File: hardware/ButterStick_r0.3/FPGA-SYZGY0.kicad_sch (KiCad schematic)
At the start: 1 part, among them U4 ECP5UM5G_85_CABGA381

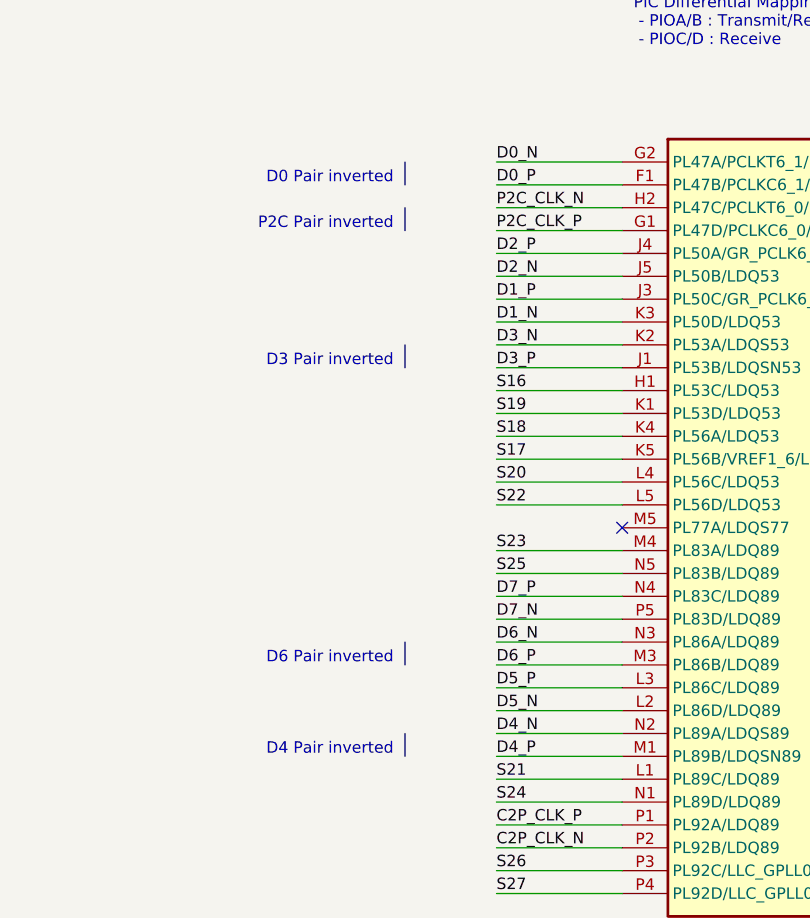
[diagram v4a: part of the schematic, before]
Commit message: hw.r0d3: Length matched all SYZYGY ports
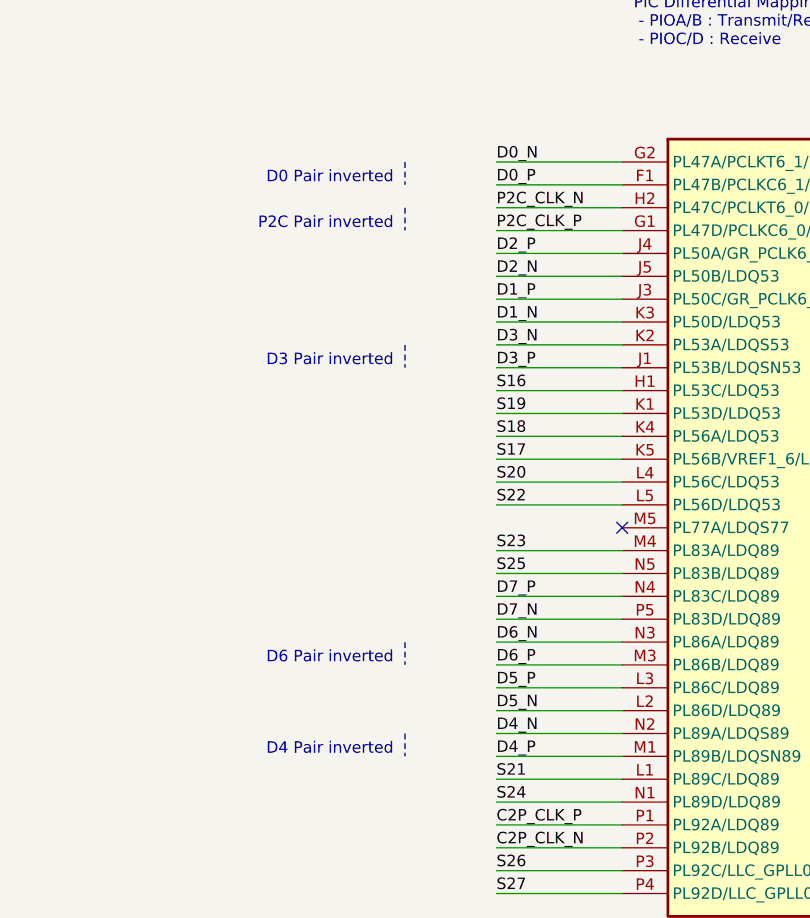
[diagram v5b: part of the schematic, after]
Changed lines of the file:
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@@
-(kicad_sch (version 20200512) (host eeschema "5.99.0-unknown-711fc99~101~ubuntu18.04.1")
+(kicad_sch (version 20200608) (host eeschema "5.99.0-unknown-08c61e6~101~ubuntu18.04.1")
   (page 1 19)
   (paper "A4")
   (no_connect (at 132.08 109.22))
   (bus_entry (at 116.84 49.53) (size 2.54 -2.54))
-  (wire (pts (xy 118.11 68.58) (xy 132.08 68.58)))
-  (wire (pts (xy 118.11 71.12) (xy 132.08 71.12)))
-  (wire (pts (xy 118.11 73.66) (xy 132.08 73.66)))
-  (wire (pts (xy 118.11 76.2) (xy 132.08 76.2)))
-  (wire (pts (xy 118.11 78.74) (xy 132.08 78.74)))
-  (wire (pts (xy 118.11 81.28) (xy 132.08 81.28)))
-  (wire (pts (xy 118.11 83.82) (xy 132.08 83.82)))
-  (wire (pts (xy 118.11 86.36) (xy 132.08 86.36)))
-  (wire (pts (xy 118.11 88.9) (xy 132.08 88.9)))
-  (wire (pts (xy 118.11 91.44) (xy 132.08 91.44)))
-  (wire (pts (xy 118.11 93.98) (xy 132.08 93.98)))
-  (wire (pts (xy 118.11 96.52) (xy 132.08 96.52)))
-  (wire (pts (xy 118.11 99.06) (xy 132.08 99.06)))
-  (wire (pts (xy 118.11 101.6) (xy 132.08 101.6)))
-  (wire (pts (xy 118.11 104.14) (xy 132.08 104.14)))
-  (wire (pts (xy 118.11 106.68) (xy 132.08 106.68)))
-  (wire (pts (xy 118.11 111.76) (xy 132.08 111.76)))
-  (wire (pts (xy 118.11 114.3) (xy 132.08 114.3)))
-  (wire (pts (xy 118.11 116.84) (xy 132.08 116.84)))
-  (wire (pts (xy 118.11 119.38) (xy 132.08 119.38)))
-  (wire (pts (xy 118.11 121.92) (xy 132.08 121.92)))
-  (wire (pts (xy 118.11 124.46) (xy 132.08 124.46)))
-  (wire (pts (xy 118.11 127) (xy 132.08 127)))
-  (wire (pts (xy 118.11 129.54) (xy 132.08 129.54)))
-  (wire (pts (xy 118.11 132.08) (xy 132.08 132.08)))
-  (wire (pts (xy 118.11 134.62) (xy 132.08 134.62)))
-  (wire (pts (xy 118.11 137.16) (xy 132.08 137.16)))
-  (wire (pts (xy 118.11 139.7) (xy 132.08 139.7)))
-  (wire (pts (xy 118.11 142.24) (xy 132.08 142.24)))
-  (wire (pts (xy 118.11 144.78) (xy 132.08 144.78)))
-  (wire (pts (xy 118.11 147.32) (xy 132.08 147.32)))
-  (wire (pts (xy 118.11 149.86) (xy 132.08 149.86)))
-  (wire (pts (xy 119.38 46.99) (xy 170.18 46.99)))
-  (wire (pts (xy 170.18 46.99) (xy 170.18 60.96)))
-  (bus (pts (xy 45.72 49.53) (xy 119.38 49.53)))
-  (polyline (pts (xy 107.95 68.58) (xy 107.95 71.12)))
-  (polyline (pts (xy 107.95 73.66) (xy 107.95 76.2)))
-  (polyline (pts (xy 107.95 88.9) (xy 107.95 91.44)))
-  (polyline (pts (xy 107.95 121.92) (xy 107.95 124.46)))
-  (polyline (pts (xy 107.95 132.08) (xy 107.95 134.62)))
+  (wire (pts (xy 118.11 68.58) (xy 132.08 68.58))
+    (stroke (width 0) (type solid) (color 0 0 0 0))
+  )
+  (wire (pts (xy 118.11 71.12) (xy 132.08 71.12))
+    (stroke (width 0) (type solid) (color 0 0 0 0))
+  )
+  (wire (pts (xy 118.11 73.66) (xy 132.08 73.66))
+    (stroke (width 0) (type solid) (color 0 0 0 0))
+  )
+  (wire (pts (xy 118.11 76.2) (xy 132.08 76.2))
+    (stroke (width 0) (type solid) (color 0 0 0 0))
+  )
+  (wire (pts (xy 118.11 78.74) (xy 132.08 78.74))
+    (stroke (width 0) (type solid) (color 0 0 0 0))
+  )
+  (wire (pts (xy 118.11 81.28) (xy 132.08 81.28))
+    (stroke (width 0) (type solid) (color 0 0 0 0))
+  )
+  (wire (pts (xy 118.11 83.82) (xy 132.08 83.82))
+    (stroke (width 0) (type solid) (color 0 0 0 0))
+  )
+  (wire (pts (xy 118.11 86.36) (xy 132.08 86.36))
+    (stroke (width 0) (type solid) (color 0 0 0 0))
+  )
+  (wire (pts (xy 118.11 88.9) (xy 132.08 88.9))
+    (stroke (width 0) (type solid) (color 0 0 0 0))
+  )
+  (wire (pts (xy 118.11 91.44) (xy 132.08 91.44))
+    (stroke (width 0) (type solid) (color 0 0 0 0))
+  )
+  (wire (pts (xy 118.11 93.98) (xy 132.08 93.98))
+    (stroke (width 0) (type solid) (color 0 0 0 0))
+  )
+  (wire (pts (xy 118.11 96.52) (xy 132.08 96.52))
+    (stroke (width 0) (type solid) (color 0 0 0 0))
+  )
+  (wire (pts (xy 118.11 99.06) (xy 132.08 99.06))
+    (stroke (width 0) (type solid) (color 0 0 0 0))
+  )
+  (wire (pts (xy 118.11 101.6) (xy 132.08 101.6))
+    (stroke (width 0) (type solid) (color 0 0 0 0))
+  )
+  (wire (pts (xy 118.11 104.14) (xy 132.08 104.14))
+    (stroke (width 0) (type solid) (color 0 0 0 0))
+  )
+  (wire (pts (xy 118.11 106.68) (xy 132.08 106.68))
+    (stroke (width 0) (type solid) (color 0 0 0 0))
+  )
+  (wire (pts (xy 118.11 111.76) (xy 132.08 111.76))
+    (stroke (width 0) (type solid) (color 0 0 0 0))
+  )
+  (wire (pts (xy 118.11 114.3) (xy 132.08 114.3))
+    (stroke (width 0) (type solid) (color 0 0 0 0))
+  )
+  (wire (pts (xy 118.11 116.84) (xy 132.08 116.84))
+    (stroke (width 0) (type solid) (color 0 0 0 0))
+  )
+  (wire (pts (xy 118.11 119.38) (xy 132.08 119.38))
+    (stroke (width 0) (type solid) (color 0 0 0 0))
+  )
+  (wire (pts (xy 118.11 121.92) (xy 132.08 121.92))
+    (stroke (width 0) (type solid) (color 0 0 0 0))
+  )
+  (wire (pts (xy 118.11 124.46) (xy 132.08 124.46))
+    (stroke (width 0) (type solid) (color 0 0 0 0))
+  )
+  (wire (pts (xy 118.11 127) (xy 132.08 127))
+    (stroke (width 0) (type solid) (color 0 0 0 0))
+  )
+  (wire (pts (xy 118.11 129.54) (xy 132.08 129.54))
+    (stroke (width 0) (type solid) (color 0 0 0 0))
+  )
+  (wire (pts (xy 118.11 132.08) (xy 132.08 132.08))
+    (stroke (width 0) (type solid) (color 0 0 0 0))
+  )
+  (wire (pts (xy 118.11 134.62) (xy 132.08 134.62))
+    (stroke (width 0) (type solid) (color 0 0 0 0))
+  )
+  (wire (pts (xy 118.11 137.16) (xy 132.08 137.16))
+    (stroke (width 0) (type solid) (color 0 0 0 0))
+  )
+  (wire (pts (xy 118.11 139.7) (xy 132.08 139.7))
+    (stroke (width 0) (type solid) (color 0 0 0 0))
+  )
+  (wire (pts (xy 118.11 142.24) (xy 132.08 142.24))
+    (stroke (width 0) (type solid) (color 0 0 0 0))
+  )
+  (wire (pts (xy 118.11 144.78) (xy 132.08 144.78))
+    (stroke (width 0) (type solid) (color 0 0 0 0))
+  )
+  (wire (pts (xy 118.11 147.32) (xy 132.08 147.32))
+    (stroke (width 0) (type solid) (color 0 0 0 0))
+  )
+  (wire (pts (xy 118.11 149.86) (xy 132.08 149.86))
+    (stroke (width 0) (type solid) (color 0 0 0 0))
+  )
+  (wire (pts (xy 119.38 46.99) (xy 170.18 46.99))
+    (stroke (width 0) (type solid) (color 0 0 0 0))
+  )
+  (wire (pts (xy 170.18 46.99) (xy 170.18 60.96))
+    (stroke (width 0) (type solid) (color 0 0 0 0))
+  )
+  (bus (pts (xy 45.72 49.53) (xy 119.38 49.53))
+    (stroke (width 0) (type solid) (color 0 0 0 0))
+  )
+  (polyline (pts (xy 107.95 68.58) (xy 107.95 71.12))
+    (stroke (width 0) (type dash) (color 0 0 0 0))
+  )
+  (polyline (pts (xy 107.95 73.66) (xy 107.95 76.2))
+    (stroke (width 0) (type dash) (color 0 0 0 0))
+  )
+  (polyline (pts (xy 107.95 88.9) (xy 107.95 91.44))
+    (stroke (width 0) (type dash) (color 0 0 0 0))
+  )
+  (polyline (pts (xy 107.95 121.92) (xy 107.95 124.46))
+    (stroke (width 0) (type dash) (color 0 0 0 0))
+  )
+  (polyline (pts (xy 107.95 132.08) (xy 107.95 134.62))
+    (stroke (width 0) (type dash) (color 0 0 0 0))
+  )
   (text "D0 Pair inverted" (at 106.68 71.12 180)
     (effects (font (size 1.27 1.27)) (justify right bottom))
@@
   )
   (symbol (lib_id "gkl_lattice:ECP5UM5G_85_CABGA381") (at 132.08 68.58 0) (unit 6)
+    (in_bom yes) (on_board yes)
     (property "Reference" "U4" (id 0) (at 178.5874 97.5614 0)
       (effects (font (size 1.524 1.524)) (justify left))

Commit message: hw.r0d3: complete first pass of routing
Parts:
- added C25: 100nF, Capacitor_SMD:C_0402_1005Metric, symbol Device:C
- added C26: 10nF, Capacitor_SMD:C_0402_1005Metric, symbol Device:C
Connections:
- net VIO1: now also C25.1, C26.1
- new net GND: C25.2, C26.2
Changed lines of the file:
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@@
-(kicad_sch (version 20200608) (host eeschema "5.99.0-unknown-08c61e6~101~ubuntu18.04.1")
-  (page 1 19)
+(kicad_sch (version 20200618) (host eeschema "5.99.0-unknown-476558e~101~ubuntu18.04.1")
+  (page 9 19)
   (paper "A4")
+  (junction (at 170.18 53.34) (diameter 0) (color 0 0 0 0))
+  (junction (at 179.07 59.69) (diameter 0) (color 0 0 0 0))
   (no_connect (at 132.08 109.22))
-  (bus_entry (at 116.84 49.53) (size 2.54 -2.54))
+  (bus_entry (at 116.84 49.53) (size 2.54 -2.54)
+    (stroke (width 0.1524) (type solid) (color 0 0 0 0))
+  )
   (wire (pts (xy 118.11 68.58) (xy 132.08 68.58))
     (stroke (width 0) (type solid) (color 0 0 0 0))
@@
     (stroke (width 0) (type solid) (color 0 0 0 0))
   )
-  (wire (pts (xy 170.18 46.99) (xy 170.18 60.96))
+  (wire (pts (xy 170.18 46.99) (xy 170.18 53.34))
+    (stroke (width 0) (type solid) (color 0 0 0 0))
+  )
+  (wire (pts (xy 170.18 53.34) (xy 170.18 60.96))
+    (stroke (width 0) (type solid) (color 0 0 0 0))
+  )
+  (wire (pts (xy 170.18 53.34) (xy 179.07 53.34))
+    (stroke (width 0) (type solid) (color 0 0 0 0))
+  )
+  (wire (pts (xy 179.07 53.34) (xy 179.07 59.69))
+    (stroke (width 0) (type solid) (color 0 0 0 0))
+  )
+  (wire (pts (xy 179.07 59.69) (xy 179.07 60.96))
+    (stroke (width 0) (type solid) (color 0 0 0 0))
+  )
+  (wire (pts (xy 179.07 59.69) (xy 189.23 59.69))
+    (stroke (width 0) (type solid) (color 0 0 0 0))
+  )
+  (wire (pts (xy 179.07 68.58) (xy 179.07 69.85))
+    (stroke (width 0) (type solid) (color 0 0 0 0))
+  )
+  (wire (pts (xy 189.23 60.96) (xy 189.23 59.69))
+    (stroke (width 0) (type solid) (color 0 0 0 0))
+  )
+  (wire (pts (xy 189.23 69.85) (xy 189.23 68.58))
     (stroke (width 0) (type solid) (color 0 0 0 0))
   )
@@
     (effects (font (size 1.27 1.27)) (justify right))
   )
+  (symbol (lib_id "gkl_power:GND") (at 179.07 69.85 0) (unit 1)
+    (in_bom yes) (on_board yes)
+    (property "Reference" "#PWR0210" (id 0) (at 179.07 76.2 0)
+      (effects (font (size 1.27 1.27)) hide)
+    )
+    (property "Value" "GND" (id 1) (at 179.1462 73.0504 0))
+    (property "Footprint" "" (id 2) (at 176.53 78.74 0)
+      (effects (font (size 1.27 1.27)) hide)
+    )
+    (property "Datasheet" "" (id 3) (at 179.07 69.85 0)
+      (effects (font (size 1.27 1.27)) hide)
+    )
+  )
+  (symbol (lib_id "gkl_power:GND") (at 189.23 69.85 0) (unit 1)
+    (in_bom yes) (on_board yes)
+    (property "Reference" "#PWR0211" (id 0) (at 189.23 76.2 0)
+      (effects (font (size 1.27 1.27)) hide)
+    )
+    (property "Value" "GND" (id 1) (at 189.3062 73.0504 0))
+    (property "Footprint" "" (id 2) (at 186.69 78.74 0)
+      (effects (font (size 1.27 1.27)) hide)
+    )
+    (property "Datasheet" "" (id 3) (at 189.23 69.85 0)
+      (effects (font (size 1.27 1.27)) hide)
+    )
+  )
+  (symbol (lib_id "Device:C") (at 179.07 64.77 0) (unit 1)
+    (in_bom yes) (on_board yes)
+    (property "Reference" "C25" (id 0) (at 180.34 62.23 0)
+      (effects (font (size 1.27 1.27)) (justify left))
+    )
+    (property "Value" "100nF" (id 1) (at 180.34 67.31 0)
+      (effects (font (size 1.27 1.27)) (justify left))
+    )
+    (property "Footprint" "Capacitor_SMD:C_0402_1005Metric" (id 2) (at 180.0352 68.58 0)
+      (effects (font (size 1.27 1.27)) hide)
+    )
+    (property "Datasheet" "" (id 3) (at 179.07 64.77 0)
+      (effects (font (size 1.27 1.27)) hide)
+    )
+    (property "SN-DK" "1276-1002-1-ND" (id 4) (at 29.21 241.3 0)
+      (effects (font (size 1.27 1.27)) hide)
+    )
+    (property "PN" "CL05B104KP5NNNC" (id 5) (at 29.21 241.3 0)
+      (effects (font (size 1.27 1.27)) hide)
+    )
+    (property "Mfg" "Samsung Electro-Mechanics" (id 6) (at 31.75 240.03 0)
+      (effects (font (size 1.27 1.27)) hide)
+    )
+  )
+  (symbol (lib_id "Device:C") (at 189.23 64.77 0) (unit 1)
+    (in_bom yes) (on_board yes)
+    (property "Reference" "C26" (id 0) (at 190.5 62.23 0)
+      (effects (font (size 1.27 1.27)) (justify left))
+    )
+    (property "Value" "10nF" (id 1) (at 190.5 67.31 0)
+      (effects (font (size 1.27 1.27)) (justify left))
+    )
+    (property "Footprint" "Capacitor_SMD:C_0402_1005Metric" (id 2) (at 190.1952 68.58 0)
+      (effects (font (size 1.27 1.27)) hide)
+    )
+    (property "Datasheet" "" (id 3) (at 189.23 64.77 0)
+      (effects (font (size 1.27 1.27)) hide)
+    )
+    (property "SN-DK" "1276-1002-1-ND" (id 4) (at 39.37 241.3 0)
+      (effects (font (size 1.27 1.27)) hide)
+    )
+    (property "PN" "CL05B103KP5NNNC" (id 5) (at 39.37 241.3 0)
+      (effects (font (size 1.27 1.27)) hide)
+    )
+    (property "Mfg" "Samsung Electro-Mechanics" (id 6) (at 31.75 240.03 0)
+      (effects (font (size 1.27 1.27)) hide)
+    )
+  )
   (symbol (lib_id "gkl_lattice:ECP5UM5G_85_CABGA381") (at 132.08 68.58 0) (unit 6)
